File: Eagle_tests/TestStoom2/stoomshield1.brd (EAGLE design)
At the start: 108.9 x 94 mm, 33 parts, among them IC1 74HC245N

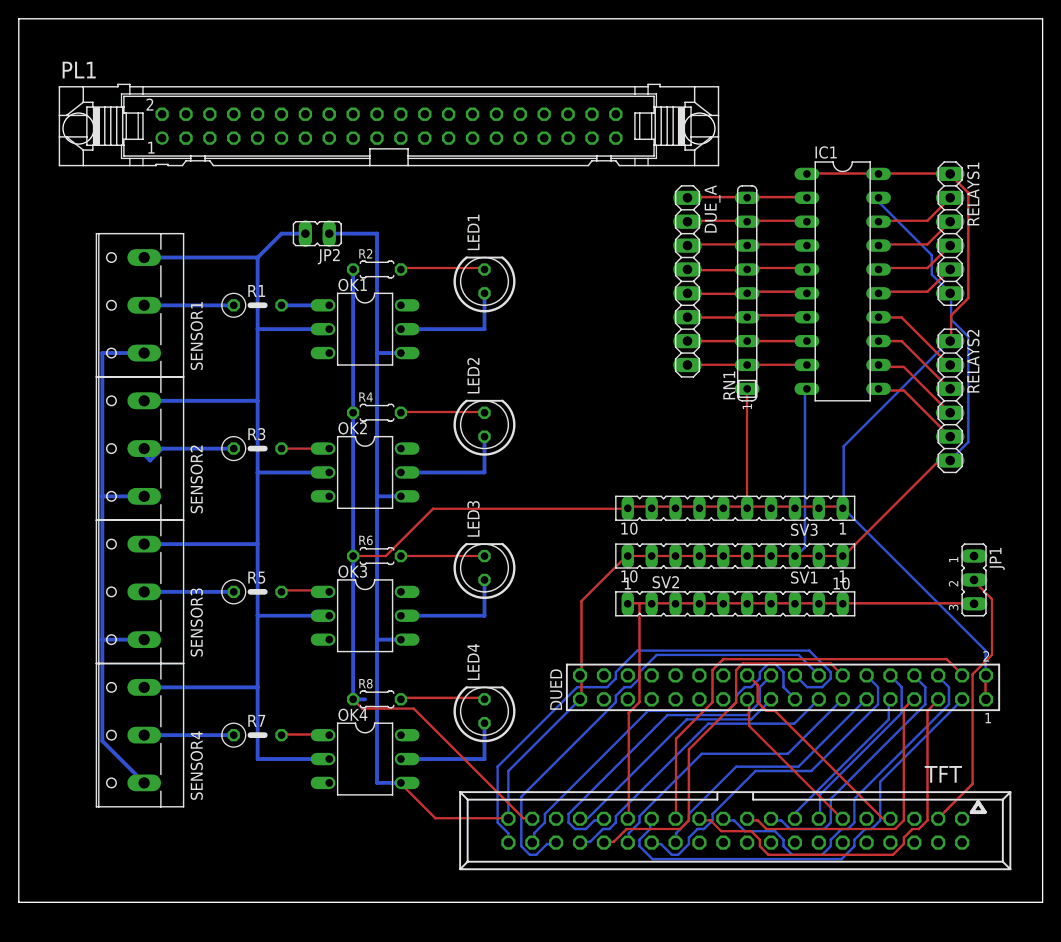
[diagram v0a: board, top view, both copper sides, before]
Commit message: Hardware test: improved eagle pcb (100x80mm) with sensor leds.
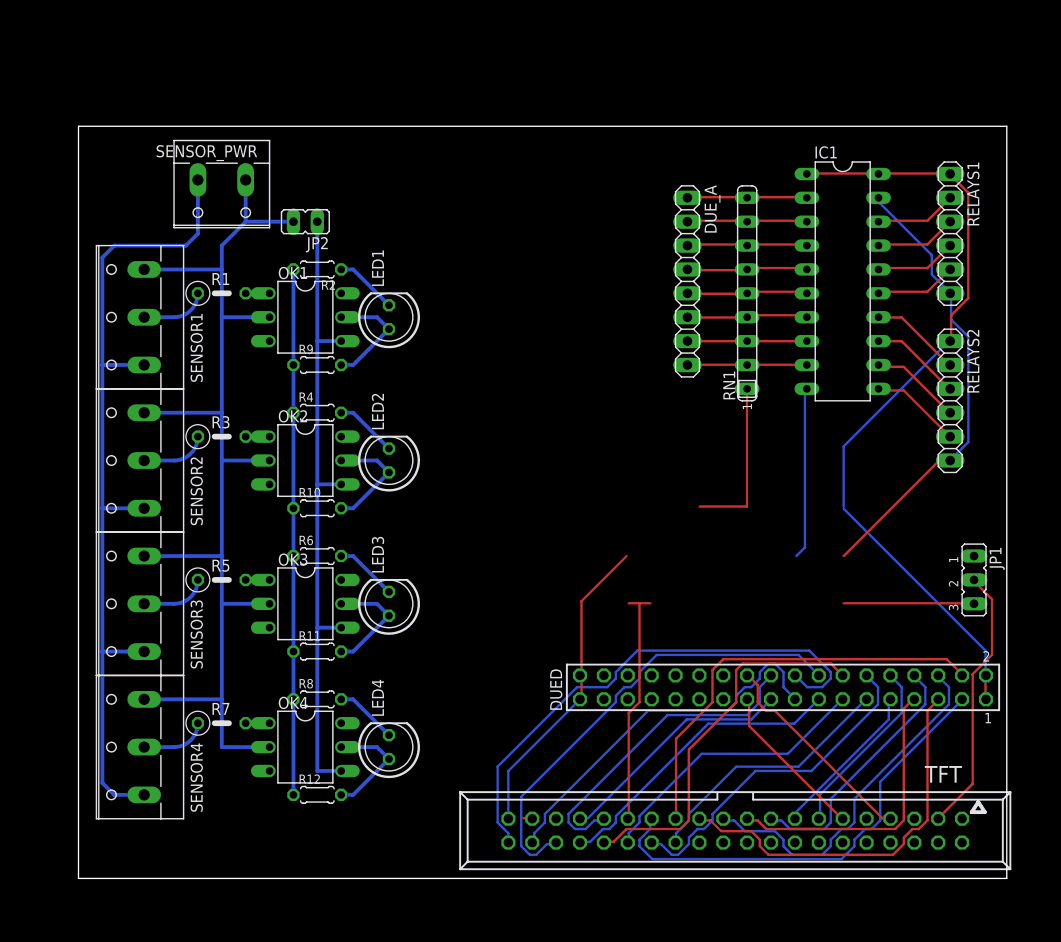
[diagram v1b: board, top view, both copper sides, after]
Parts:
- removed PL1: (no value), con-harting-v:40V
- removed SV1, SV2, SV3: (no value), con-lsta:FE10
- added R10, R11, R12, R9: 10000, resistor:0204/5
- added SENSOR_PWR: (no value), con-wago-508:W237-132
- moved LED1 10.9 mm to (33.0, 59.7)
- moved LED3 10.9 mm to (33.0, 29.2)
- moved LED4 10.9 mm to (33.0, 14.0)
- moved LED2 10.9 mm to (33.0, 44.5)
- moved OK2 6.48 mm to (24.1, 44.5)
- moved OK3 6.48 mm to (24.1, 29.2)
- moved OK4 6.48 mm to (24.1, 14.0)
- moved OK1 6.48 mm to (24.1, 59.7)
- moved R2 6.35 mm to (25.4, 64.8), turned to 180 degrees
- moved R4 6.35 mm to (25.4, 49.5)
- moved R6 6.35 mm to (25.4, 34.3)
- moved R8 6.35 mm to (25.4, 19.1)
- moved R3 4.02 mm to (15.2, 47.0)
- moved R7 4.02 mm to (15.2, 16.5)
- moved R5 4.02 mm to (15.2, 31.8)
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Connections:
- net +24V: now also SENSOR_PWR.2
- net +3V3: no longer SV2.1, SV2.10, SV2.2, SV2.3, SV2.4, SV2.5, SV2.6, SV2.7, SV2.8, SV2.9
- net +5V: now also R10.1, R11.1, R12.1, R2.2, R9.1; no longer R2.1, SV3.1, SV3.10, SV3.2, SV3.3, SV3.4, SV3.5, SV3.6, SV3.7, SV3.8, SV3.9
- net DUE_SENSOR1: now also R9.2
- net DUE_SENSOR2: now also R10.2
- net DUE_SENSOR3: now also R11.2
- net DUE_SENSOR4: now also R12.2
- net GND: no longer SV1.1, SV1.10, SV1.2, SV1.3, SV1.4, SV1.5, SV1.6, SV1.7, SV1.8, SV1.9
- net GND1: now also SENSOR_PWR.1
- net N$5: now also R2.1; no longer R2.2
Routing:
- net +5V: track 223.8 -> 158.1 mm
- net GND: track 209.8 -> 168.4 mm
- net +24V: track 60.9 -> 91.1 mm
- net +3V3: track 60.6 -> 39.6 mm
- net GND1: track 138.2 -> 119.8 mm
- net N$7: track 11.8 -> 6.77 mm
- net N$3: track 9.53 -> 6.77 mm
- net N$13: track 9.53 -> 6.77 mm
- net N$10: track 9.53 -> 6.77 mm
- net N$6: track 5.08 -> 2.54 mm
- net N$4: track 5.08 -> 2.54 mm
- net N$9: track 5.21 -> 2.74 mm
- net N$5: track 9.09 -> 6.66 mm
- net N$14: track 9.09 -> 6.66 mm
- net N$12: track 5.12 -> 2.69 mm
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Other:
- board size 108.9 x 94 mm -> 98.7 x 80 mm

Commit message: Hardware test: improved eagle pcb screw contact wiring.
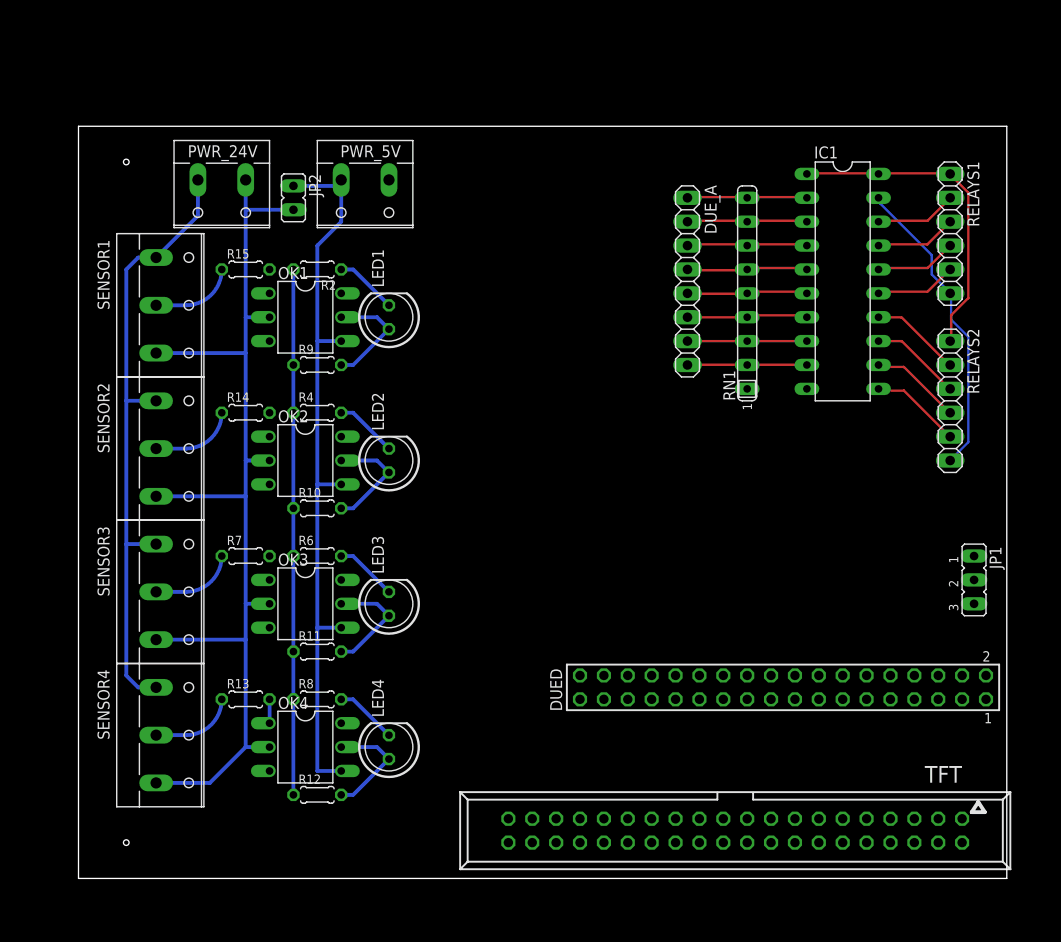
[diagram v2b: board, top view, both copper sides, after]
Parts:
- removed R1, R3, R5: 1500, resistor:0207/5V
- added PWR_5V: (no value), con-wago-508:W237-132
- added R13, R14, R15: 1500, resistor:0204/5
- R2, R4, R6, R8: value (none) -> 65
- R7: device resistor:0207/5V -> resistor:0204/5
- moved R7 18.0 mm to (17.8, 34.3)
- moved JP2 2.84 mm to (22.9, 72.4), turned to 180 degrees
- moved SENSOR1 2.84 mm to (8.89, 61.0), turned to 270 degrees
- moved SENSOR3 2.84 mm to (8.89, 30.5), turned to 270 degrees
- moved SENSOR4 2.84 mm to (8.89, 15.2), turned to 270 degrees
- moved SENSOR2 2.84 mm to (8.89, 45.7), turned to 270 degrees
- renumbered SENSOR_PWR to PWR_24V
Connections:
- net +5V: now also PWR_5V.1
- net GND: now also PWR_5V.2
- net N$10: now also R7.1; no longer R5.1
- net N$12: now also R13.2; no longer R7.2
- net N$13: now also R13.1; no longer R7.1
- net N$3: now also R15.1; no longer R1.1
- net N$4: now also R15.2; no longer R1.2
- net N$6: now also R14.2; no longer R3.2
- net N$7: now also R14.1; no longer R3.1
- net N$9: now also R7.2; no longer R5.2
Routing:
- net +5V: track 158.1 -> 91.0 mm
- net GND: track 168.4 -> 112.3 mm
- net DB0: track 55.8 -> 0.00 mm
- net DB2: track 49.5 -> 0.00 mm
- net DB8: track 48.2 -> 0.00 mm
- net DB9: track 45.2 -> 0.00 mm
- net DB10: track 41.6 -> 0.00 mm
- net DB1: track 40.2 -> 0.00 mm
- net DB4: track 40.2 -> 0.00 mm
- net +3V3: track 39.6 -> 0.16 mm
- net DB11: track 38.1 -> 0.00 mm
- net DB6: track 35.7 -> 0.00 mm
- net WR: track 34.0 -> 0.00 mm
- net DB3: track 32.1 -> 0.00 mm
- net DB12: track 30.9 -> 0.00 mm
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
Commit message: Hardware test: improved eagle pcb+schema for relay.
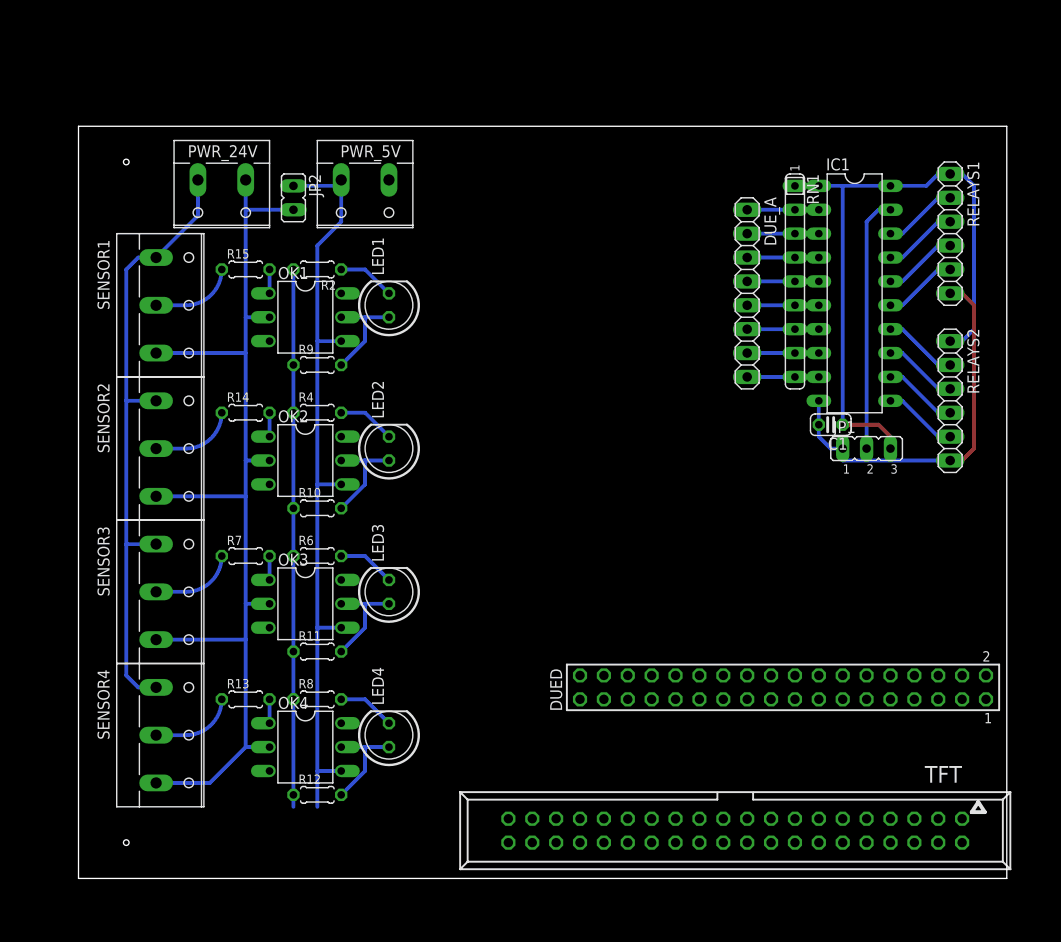
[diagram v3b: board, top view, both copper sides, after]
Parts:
- added C1: (no value), rcl:C025-024X044
- moved JP1 18.1 mm to (83.8, 45.7), turned to 0 degrees
- moved DUE_A 6.48 mm to (71.1, 62.2)
- moved RN1 5.24 mm to (76.2, 63.5), turned to 270 degrees
- moved IC1 1.80 mm to (82.5, 62.2)
- moved LED1 1.27 mm to (33.0, 61.0)
- moved LED3 1.27 mm to (33.0, 30.5)
- moved LED4 1.27 mm to (33.0, 15.2)
- moved LED2 1.27 mm to (33.0, 45.7)
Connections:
- removed net N$2: JP1.1
- net +3V3: now also TFT.3; no longer JP1.3
- net +5V: now also C1.1, JP1.3
- net GND: now also C1.2, JP1.1; no longer IC1.19
- net KLEP1_SIG: now also RN1.2; no longer RN1.9
- net KLEP2_SIG: now also RN1.3; no longer RN1.8
- net KLEP3_SIG: now also RN1.4; no longer RN1.7
- net KLEP4_SIG: now also RN1.5; no longer RN1.6
- net KLEP5_SIG: now also RN1.6; no longer RN1.5
- net KLEP6_SIG: now also RN1.7; no longer RN1.4
- net KLEP7_SIG: now also RN1.8; no longer RN1.3
- net KLEP8_SIG: now also RN1.9; no longer RN1.2
- net N$1: now also IC1.19; no longer TFT.3
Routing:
- net +5V: track 91.0 -> 128.1 mm
- net N$1: track 0.00 -> 27.2 mm
- net GND: track 112.3 -> 125.7 mm
- net KLEP3_SIG: track 12.9 -> 7.62 mm
- net KLEP6_SIG: track 12.9 -> 7.62 mm
- net KLEP4_SIG: track 12.9 -> 7.62 mm
- net KLEP5_SIG: track 12.9 -> 7.62 mm
- net KLEP2_SIG: track 12.9 -> 7.62 mm
- net KLEP1_SIG: track 12.8 -> 7.62 mm
- net KLEP8_SIG: track 12.7 -> 7.62 mm
- net KLEP7_SIG: track 12.7 -> 7.62 mm
- net N$9: track 0.00 -> 2.54 mm
- net N$6: track 0.00 -> 2.54 mm
- net N$4: track 0.00 -> 2.54 mm
- net KLEP7: track 9.72 -> 7.93 mm
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
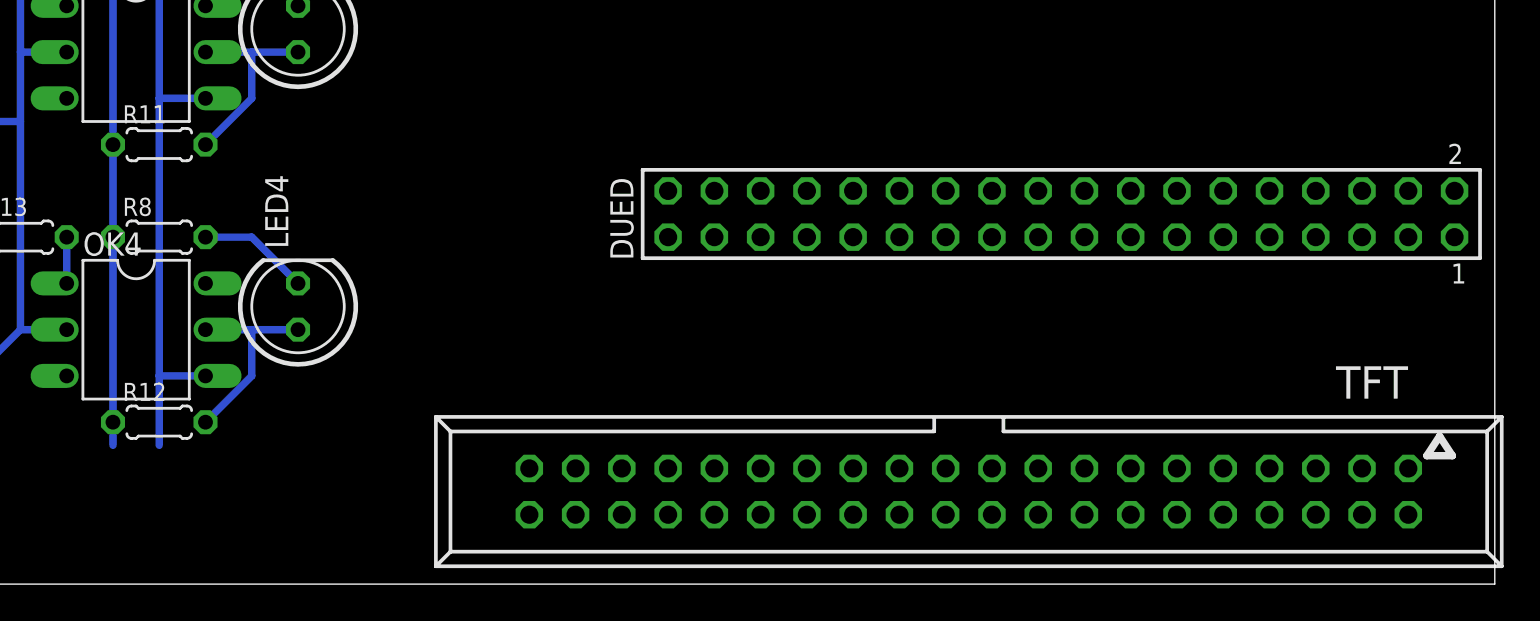
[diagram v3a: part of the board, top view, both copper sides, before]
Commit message: Hardware test: aproximated eagle pcb TFT connector placement.
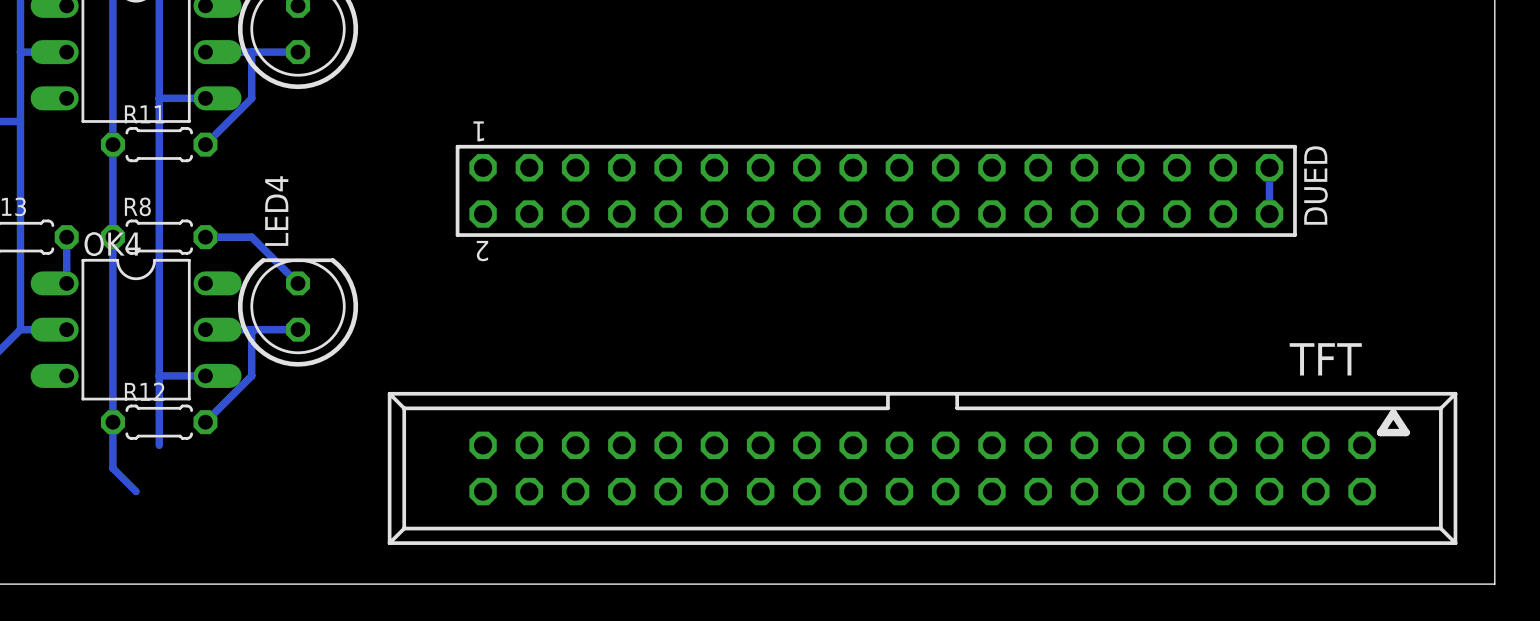
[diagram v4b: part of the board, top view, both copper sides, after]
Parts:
- moved DUED 10.2 mm to (64.8, 21.6), turned to 180 degrees
- moved TFT 2.84 mm to (67.3, 6.35)
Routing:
- net +5V: track 128.1 -> 130.9 mm
- net GND: track 125.7 -> 128.0 mm

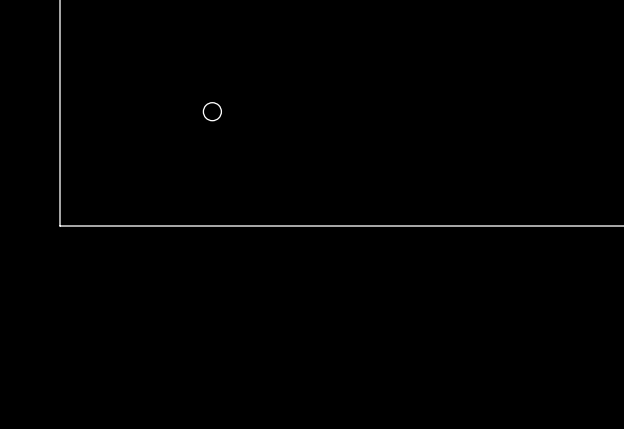
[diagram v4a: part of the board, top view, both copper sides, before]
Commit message: Hardware schema: Fixed RS pull-up.
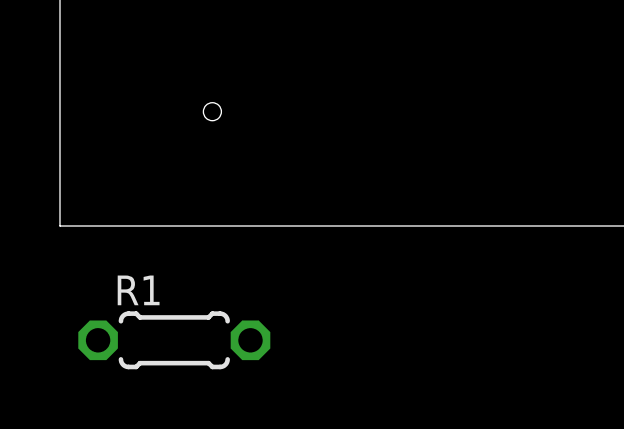
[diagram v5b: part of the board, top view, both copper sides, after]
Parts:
- added R1: 10000, resistor:0204/5
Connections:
- new net N$2: R1.2, TFT.29
- net +3V3: now also R1.1; no longer TFT.29
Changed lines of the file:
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@@
 <element name="C1" library="rcl" package="C025-024X044" value="" x="80.01" y="48.26" rot="R180"/>
 <element name="JP1" library="jumper" package="JP2" value="" x="83.82" y="45.72"/>
+<element name="R1" library="resistor" package="0204/5" value="10000" x="3.81" y="-3.81"/>
 </elements>
 <signals>
@@
 </signal>
 <signal name="+3V3">
-<contactref element="TFT" pad="29"/>
 <contactref element="TFT" pad="3"/>
-<wire x1="55.88" y1="7.62" x2="88.9" y2="7.62" width="0" layer="19" extent="1-1"/>
+<contactref element="R1" pad="1"/>
+<wire x1="1.27" y1="-3.81" x2="88.9" y2="7.62" width="0" layer="19" extent="1-1"/>
 </signal>
 <signal name="GND1">
@@
 <wire x1="83.82" y1="69.85" x2="83.82" y2="45.72" width="0.4064" layer="16"/>
 </signal>
+<signal name="N$2">
+<contactref element="R1" pad="2"/>
+<contactref element="TFT" pad="29"/>
+<wire x1="6.35" y1="-3.81" x2="55.88" y2="7.62" width="0" layer="19" extent="1-1"/>
+</signal>
 </signals>
